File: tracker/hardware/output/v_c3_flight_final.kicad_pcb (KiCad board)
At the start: 4 copper layers, 55 x 45 mm, 20 parts, among them J1 Prog_Header, J2 Debug_Header, U1 ESP32-C3-WROOM-02, U2 LR2021F33, U3 MAX-M10S, U4 TPS7A02, U5 BMP280

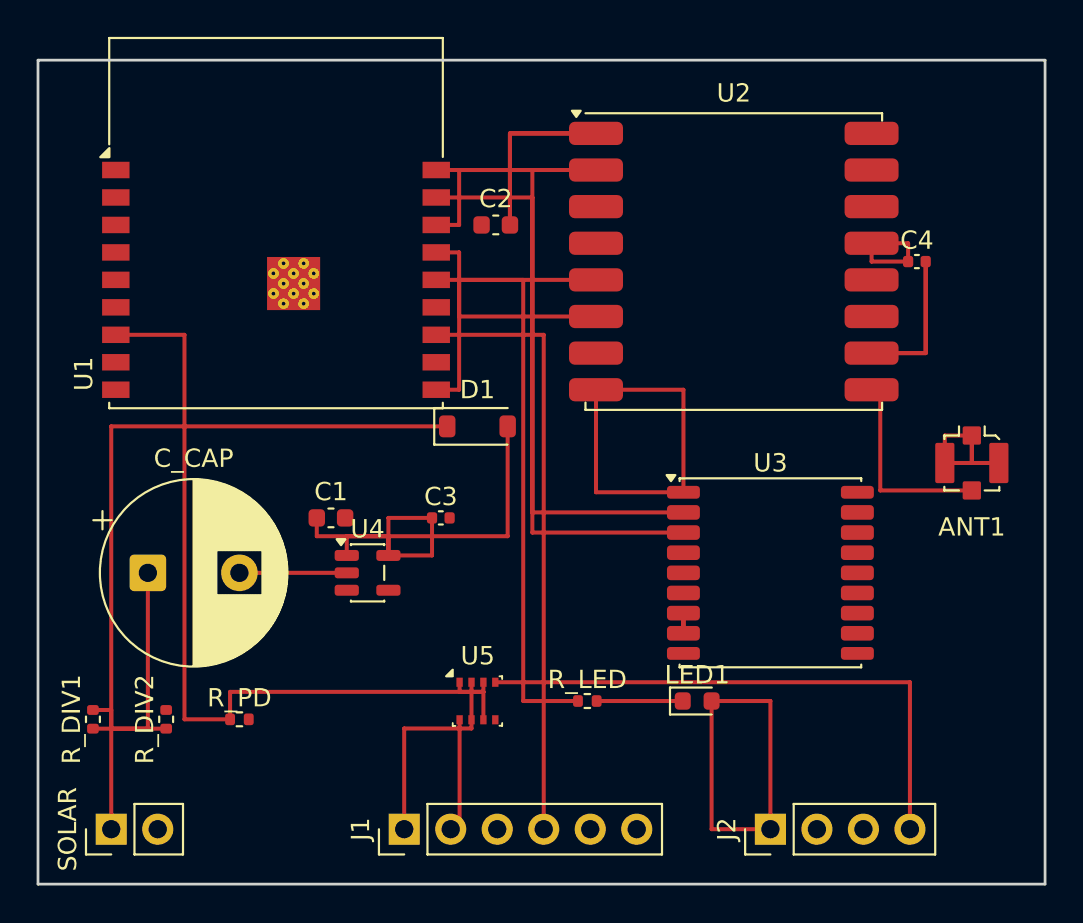
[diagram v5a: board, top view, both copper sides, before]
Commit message: fix: C3 flight PCB layer assignment — 8→1 shorting_items, 55→44 violations
Moved crossing tracks to B.Cu (33 on F.Cu, 33 on B.Cu)
DRC: 1 shorting_items, 12 tracks_crossing (B.Cu-vs-B.Cu), 14 dangling
Gerbers: F_Cu=13.6KB, B_Cu=2.5KB, all planes populated
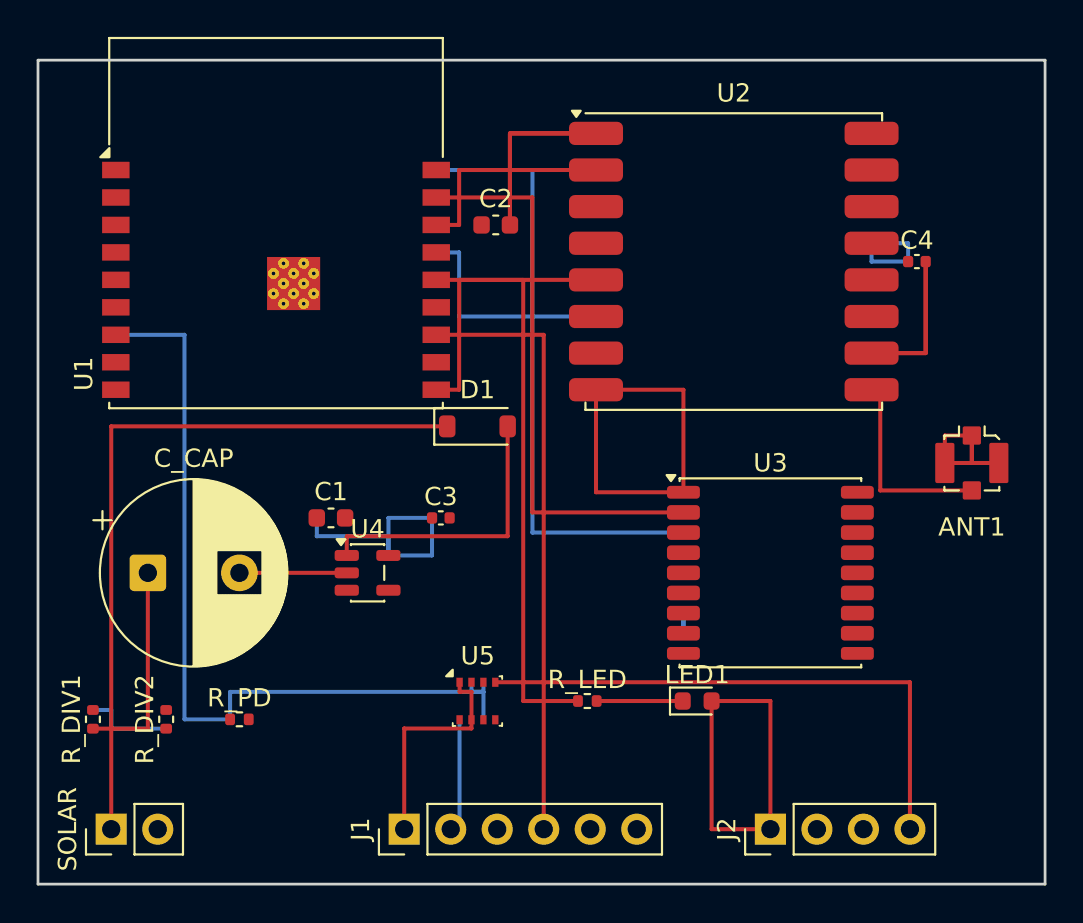
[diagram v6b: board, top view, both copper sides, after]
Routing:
- net I2C_SDA: track 43.1 -> 0.00 mm
- net +3V3: track 32.2 -> 75.3 mm
- net GPS_TX: track 33.3 -> 45.5 mm
- net LR_RST: track 12.2 -> 0.00 mm
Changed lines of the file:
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@@
 		(end 23.025 42)
 		(width 0.22)
-		(layer "F.Cu")
+		(layer "B.Cu")
 		(net 1)
 	)
@@
 		(end 35.25 31.3)
 		(width 0.22)
-		(layer "F.Cu")
+		(layer "B.Cu")
 		(net 1)
 	)
@@
 		(end 24.325 36.025)
 		(width 0.22)
-		(layer "F.Cu")
+		(layer "B.Cu")
+		(net 1)
+	)
+	(segment
+		(start 8 36)
+		(end 8 15)
+		(width 0.22)
+		(layer "B.Cu")
 		(net 1)
 	)
@@
 		(end 47.52 10)
 		(width 0.22)
-		(layer "F.Cu")
+		(layer "B.Cu")
 		(net 1)
 	)
@@
 		(end 45.525 10)
 		(width 0.22)
-		(layer "F.Cu")
+		(layer "B.Cu")
+		(net 1)
+	)
+	(segment
+		(start 10.49 34.5)
+		(end 10.49 36)
+		(width 0.22)
+		(layer "B.Cu")
+		(net 1)
+	)
+	(segment
+		(start 8 15)
+		(end 4.25 15)
+		(width 0.22)
+		(layer "B.Cu")
+		(net 1)
+	)
+	(segment
+		(start 24.325 34.5)
+		(end 10.49 34.5)
+		(width 0.22)
+		(layer "B.Cu")
 		(net 1)
 	)
@@
 		(end 45.525 11)
 		(width 0.22)
-		(layer "F.Cu")
+		(layer "B.Cu")
 		(net 1)
 	)
@@
 		(end 21.52 27.05)
 		(width 0.22)
-		(layer "F.Cu")
+		(layer "B.Cu")
 		(net 1)
 	)
@@
 		(end 24.325 34.5)
 		(width 0.22)
-		(layer "F.Cu")
+		(layer "B.Cu")
 		(net 1)
 	)
@@
 		(end 19.1375 25)
 		(width 0.22)
-		(layer "F.Cu")
+		(layer "B.Cu")
 		(net 1)
 	)
@@
 		(end 19.1375 26)
 		(width 0.22)
-		(layer "F.Cu")
+		(layer "B.Cu")
 		(net 1)
 	)
@@
 		(end 23.675 34.5)
 		(width 0.22)
-		(layer "F.Cu")
+		(layer "B.Cu")
 		(net 1)
 	)
@@
 		(end 21.52 25)
 		(width 0.22)
-		(layer "F.Cu")
+		(layer "B.Cu")
 		(net 1)
 	)
@@
 		(end 23.025 36.025)
 		(width 0.22)
-		(layer "F.Cu")
+		(layer "B.Cu")
 		(net 1)
 	)
@@
 		(end 15.225 26)
 		(width 0.22)
-		(layer "F.Cu")
+		(layer "B.Cu")
 		(net 1)
 	)
@@
 		(end 19.1375 27.05)
 		(width 0.22)
-		(layer "F.Cu")
+		(layer "B.Cu")
 		(net 1)
 	)
@@
 		(end 35.25 30.2)
 		(width 0.22)
-		(layer "F.Cu")
+		(layer "B.Cu")
 		(net 1)
 	)
@@
 		(end 19.1375 27.05)
 		(width 0.22)
-		(layer "F.Cu")
+		(layer "B.Cu")
+		(net 1)
+	)
+	(segment
+		(start 24.325 33.975)
+		(end 24.325 34.5)
+		(width 0.22)
+		(layer "B.Cu")
 		(net 1)
 	)
@@
 		(end 47.52 11)
 		(width 0.22)
-		(layer "F.Cu")
+		(layer "B.Cu")
+		(net 1)
+	)
+	(segment
+		(start 10.49 36)
+		(end 8 36)
+		(width 0.22)
+		(layer "B.Cu")
 		(net 1)
 	)
@@
 		(end 4 36.51)
 		(width 0.22)
-		(layer "F.Cu")
+		(layer "B.Cu")
 		(net 5)
 	)
@@
 		(end 7 36.51)
 		(width 0.22)
-		(layer "F.Cu")
+		(layer "B.Cu")
 		(net 5)
 	)
@@
 		(end 4 35.49)
 		(width 0.22)
-		(layer "F.Cu")
+		(layer "B.Cu")
 		(net 5)
 	)
@@
 		(end 27 6)
 		(width 0.22)
-		(layer "F.Cu")
+		(layer "B.Cu")
+		(net 7)
+	)
+	(segment
+		(start 23 14)
+		(end 23 10.5)
+		(width 0.22)
+		(layer "B.Cu")
+		(net 7)
+	)
+	(segment
+		(start 30.475 14)
+		(end 23 14)
+		(width 0.22)
+		(layer "B.Cu")
 		(net 7)
 	)
@@
 		(end 27 25.8)
 		(width 0.22)
-		(layer "F.Cu")
+		(layer "B.Cu")
+		(net 7)
+	)
+	(segment
+		(start 23 10.5)
+		(end 21.75 10.5)
+		(width 0.22)
+		(layer "B.Cu")
 		(net 7)
 	)
@@
 		(end 35.25 25.8)
 		(width 0.22)
-		(layer "F.Cu")
+		(layer "B.Cu")
 		(net 7)
 	)
@@
 	)
 	(segment
-		(start 23 14)
-		(end 23 10.5)
-		(width 0.22)
-		(layer "F.Cu")
-		(net 13)
-	)
-	(segment
-		(start 30.475 14)
-		(end 23 14)
-		(width 0.22)
-		(layer "F.Cu")
-		(net 13)
-	)
-	(segment
-		(start 23 10.5)
-		(end 21.75 10.5)
-		(width 0.22)
-		(layer "F.Cu")
-		(net 13)
-	)
-	(segment
-		(start 8 36)
-		(end 8 15)
-		(width 0.22)
-		(layer "F.Cu")
-		(net 16)
-	)
-	(segment
-		(start 10.49 34.5)
-		(end 10.49 36)
-		(width 0.22)
-		(layer "F.Cu")
-		(net 16)
-	)
-	(segment
-		(start 8 15)
-		(end 4.25 15)
-		(width 0.22)
-		(layer "F.Cu")
-		(net 16)
-	)
-	(segment
-		(start 24.325 34.5)
-		(end 10.49 34.5)
-		(width 0.22)
-		(layer "F.Cu")
-		(net 16)
-	)
-	(segment
-		(start 24.325 33.975)
-		(end 24.325 34.5)
-		(width 0.22)
-		(layer "F.Cu")
-		(net 16)
-	)
-	(segment
-		(start 10.49 36)
-		(end 8 36)
-		(width 0.22)
-		(layer "F.Cu")
-		(net 16)
-	)
-	(segment
